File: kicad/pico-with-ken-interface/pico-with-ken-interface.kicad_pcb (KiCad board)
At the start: 4 copper layers, 81.3 x 81.3 mm, 12 parts, among them SW2 TSC015A03526A, U1 Pico, U3 XDZ254-2-15-W-2.5-G1, U5 PM254-2-15-W-8.5

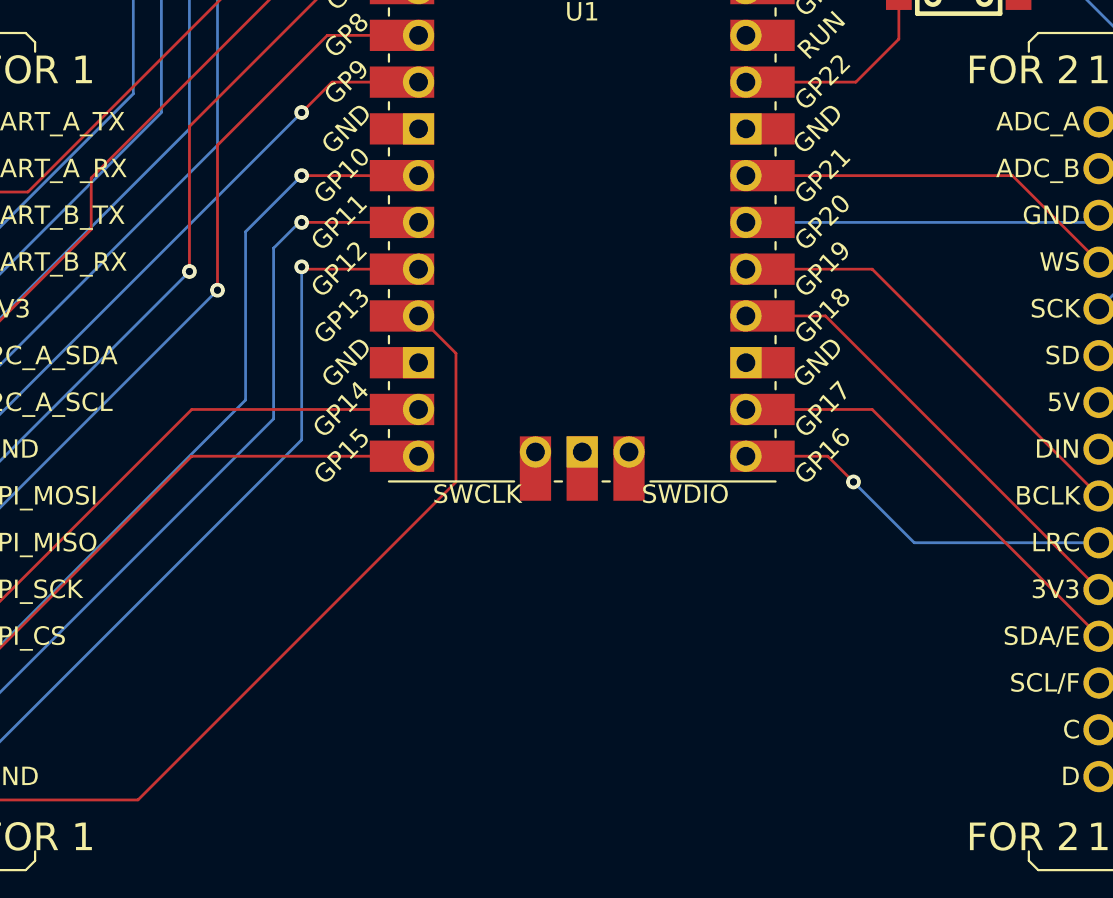
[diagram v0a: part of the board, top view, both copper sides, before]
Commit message: add labels for pico pins
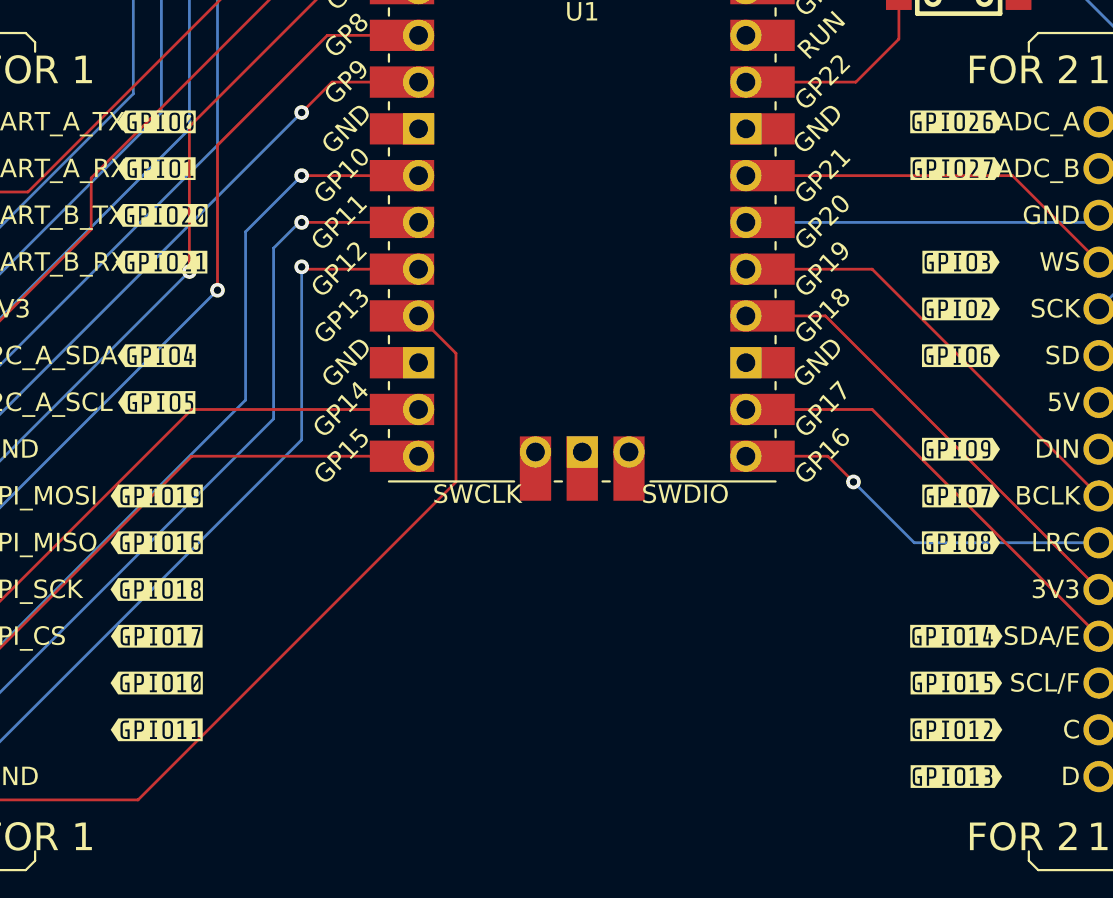
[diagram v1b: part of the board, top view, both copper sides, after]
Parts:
- added kibuzzard-69B2BBD5: G***, kibuzzard-69B2BBD5, F.Cu at (75.9, 84.1)
- added kibuzzard-69B2BBE8: G***, kibuzzard-69B2BBE8, F.Cu at (75.9, 86.6)
- added kibuzzard-69B2BC4D: G***, kibuzzard-69B2BC4D, F.Cu at (75.9, 101.9)
- added kibuzzard-69B2BC53: G***, kibuzzard-69B2BC53, F.Cu at (75.9, 99.3)
- added kibuzzard-69B2BC5B: G***, kibuzzard-69B2BC5B, F.Cu at (75.9, 96.8)
- added kibuzzard-69B2BC62: G***, kibuzzard-69B2BC62, F.Cu at (75.9, 94.2)
- added kibuzzard-69B2BC71: G***, kibuzzard-69B2BC71, F.Cu at (75.9, 91.7)
- added kibuzzard-69B2BC8C: G***, kibuzzard-69B2BC8C, F.Cu at (75.9, 71.4)
- added kibuzzard-69B2BC9C: G***, kibuzzard-69B2BC9C, F.Cu at (75.9, 73.9)
- added kibuzzard-69B2BCA8: G***, kibuzzard-69B2BCA8, F.Cu at (76.2, 76.5)
- added kibuzzard-69B2BCB2: G***, kibuzzard-69B2BCB2, F.Cu at (76.2, 79.0)
- added kibuzzard-69B2BCDF: G***, kibuzzard-69B2BCDF, F.Cu at (75.9, 104.4)
- added kibuzzard-69B2BD0A: G***, kibuzzard-69B2BD0A, F.Cu at (119.4, 71.4)
- added kibuzzard-69B2BD17: G***, kibuzzard-69B2BD17, F.Cu at (119.4, 73.9)
- added kibuzzard-69B2BD42: G***, kibuzzard-69B2BD42, F.Cu at (119.6, 79.0)
- added kibuzzard-69B2BD56: G***, kibuzzard-69B2BD56, F.Cu at (119.6, 81.5)
- added kibuzzard-69B2BD62: G***, kibuzzard-69B2BD62, F.Cu at (119.6, 84.1)
- added kibuzzard-69B2BD76: G***, kibuzzard-69B2BD76, F.Cu at (119.6, 89.2)
- added kibuzzard-69B2BD80: G***, kibuzzard-69B2BD80, F.Cu at (119.6, 91.7)
- added kibuzzard-69B2BD8D: G***, kibuzzard-69B2BD8D, F.Cu at (119.6, 94.2)
- added kibuzzard-69B2BD9D: G***, kibuzzard-69B2BD9D, F.Cu at (119.4, 99.3)
- added kibuzzard-69B2BDB2: G***, kibuzzard-69B2BDB2, F.Cu at (119.4, 101.9)
- added kibuzzard-69B2BDBA: G***, kibuzzard-69B2BDBA, F.Cu at (119.4, 104.4)
- added kibuzzard-69B2BDC4: G***, kibuzzard-69B2BDC4, F.Cu at (119.4, 106.9)

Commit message: Update pico-with-ken-interface.kicad_pcb
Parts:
- moved kibuzzard-69B2BC4D 0.25 mm to (76.2, 101.9)
- moved kibuzzard-69B2BC53 0.25 mm to (76.2, 99.3)
- moved kibuzzard-69B2BC5B 0.25 mm to (76.2, 96.8)
- moved kibuzzard-69B2BC62 0.25 mm to (76.2, 94.2)
- moved kibuzzard-69B2BC71 0.25 mm to (76.2, 91.7)
- moved kibuzzard-69B2BCA8 0.13 mm to (76.3, 76.5)
- moved kibuzzard-69B2BCB2 0.13 mm to (76.3, 79.0)
- moved kibuzzard-69B2BD42 0.13 mm to (119.8, 79.0)
- moved kibuzzard-69B2BD56 0.13 mm to (119.8, 81.5)
- moved kibuzzard-69B2BD62 0.13 mm to (119.8, 84.1)
- moved kibuzzard-69B2BD76 0.13 mm to (119.8, 89.2)
- moved kibuzzard-69B2BD80 0.13 mm to (119.8, 91.7)
- moved kibuzzard-69B2BD8D 0.13 mm to (119.8, 94.2)
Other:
- board text added: "Raspberry Pi Pico (RP2040) with KEN Interface"
- board text removed: "Raspberry Pi Pico (RP2040) with EKN Interface"

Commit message: adjust labels, send to pcb maker
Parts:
- moved kibuzzard-69B2BCDF 2.85 mm to (78.8, 104.4)
- moved kibuzzard-69B2BC4D 2.60 mm to (78.8, 101.9)
- moved kibuzzard-69B2BC53 2.60 mm to (78.8, 99.3)
- moved kibuzzard-69B2BC5B 2.60 mm to (78.8, 96.8)
- moved kibuzzard-69B2BC62 2.60 mm to (78.8, 94.2)
- moved kibuzzard-69B2BC71 2.58 mm to (78.8, 91.7)
- moved kibuzzard-69B2BBD5 2.44 mm to (78.4, 84.1)
- moved kibuzzard-69B2BBE8 2.44 mm to (78.4, 86.6)
- moved kibuzzard-69B2BC8C 2.42 mm to (78.4, 71.4)
- moved kibuzzard-69B2BC9C 2.42 mm to (78.4, 73.9)
- moved kibuzzard-69B2BCA8 2.42 mm to (78.7, 76.5)
- moved kibuzzard-69B2BCB2 2.42 mm to (78.7, 79.0)
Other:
- board text added: "version:1.0 date: 20260315"
- board text removed: "version:1.0 date: 20260312"
